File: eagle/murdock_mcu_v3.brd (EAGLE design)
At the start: 47 x 31.8 mm, 34 parts, among them IC1 MPU-9150, IC2 LT1763CS8-3.3, IC3 STM32F4XX_64, IC4 BMP085, IC5 24LC16BSN, T1 PFET, U1 USD-SOCKETNEW, X2 MURDOCK_STACK

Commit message: usb fix
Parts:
- added R7: 15k, SparkFun-Resistors:0402-RES
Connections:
- net +3V3: now also R7.1
- net +5V: now also IC3.42
- net SP_PWR: now also R7.2
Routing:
- net +5V: track 35.7 -> 56.2 mm, vias 2 -> 4
- net SP_PWR: track 20.7 -> 25.4 mm
- net +3V3: track 182.1 -> 183.5 mm
- net GND: vias 28 -> 27
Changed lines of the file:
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@@
 </element>
 <element name="C8" library="rcl" package="C0402" value="10nF" x="4.4675" y="20.49" smashed="yes" rot="R90">
-<attribute name="NAME" x="5.245" y="19.2325" size="0.8128" layer="25" font="vector" ratio="10" rot="R180"/>
+<attribute name="NAME" x="5.1675" y="21.345" size="0.8128" layer="25" font="vector" ratio="10" rot="R270"/>
 <attribute name="VALUE" x="4.7725" y="19.155" size="0.6096" layer="27" font="vector" ratio="10" rot="R90"/>
 </element>
@@
 <attribute name="NAME" x="20.095" y="17.467" size="0.8128" layer="25" font="vector" ratio="10"/>
 <attribute name="VALUE" x="22.595" y="16.963" size="1.27" layer="27"/>
+</element>
+<element name="R7" library="SparkFun-Resistors" package="0402-RES" value="15k" x="4.4" y="17.8" smashed="yes" rot="R270">
+<attribute name="NAME" x="5.0985" y="18.689" size="0.8128" layer="25" font="vector" ratio="10" rot="R270"/>
+<attribute name="VALUE" x="3.257" y="18.8795" size="0.4064" layer="27" rot="R270"/>
 </element>
 </elements>
@@
 <wire x1="39.0025" y1="12.2475" x2="37.1025" y2="12.2475" width="0.3048" layer="1"/>
 <via x="20.3" y="8.35" extent="1-16" drill="0.6"/>
-<via x="23.55" y="14.75" extent="1-16" drill="0.6"/>
 <via x="20.55" y="14.65" extent="1-16" drill="0.6"/>
 <via x="23.95" y="21.35" extent="1-16" drill="0.6"/>
@@
 <via x="32.25" y="29.8" extent="1-16" drill="0.6"/>
 <via x="36.85" y="24.5" extent="1-16" drill="0.4"/>
-<via x="24.2" y="19.2" extent="1-16" drill="0.6"/>
+<via x="24.5" y="19.1" extent="1-16" drill="0.6"/>
 <contactref element="IC4" pad="1"/>
 <via x="9.85" y="22.65" extent="1-16" drill="0.6"/>
@@
 <contactref element="X2" pad="3V3"/>
 <contactref element="C2" pad="+"/>
-<wire x1="5.715" y1="18.265" x2="5.715" y2="21.1675" width="0.6096" layer="1"/>
+<wire x1="5.715" y1="18.265" x2="5.715" y2="18.5" width="0.6096" layer="1"/>
 <contactref element="IC3" pad="48"/>
 <contactref element="IC3" pad="64"/>
@@
 <contactref element="C3" pad="1"/>
 <contactref element="U1" pad="4"/>
+<wire x1="5.715" y1="18.5" x2="5.715" y2="21.1675" width="0.6096" layer="1"/>
 <wire x1="5.715" y1="21.1675" x2="5.715" y2="23.185" width="0.6096" layer="1"/>
 <wire x1="34.4525" y1="16.0975" x2="34.4525" y2="17.1975" width="0.3048" layer="1"/>
@@
 <via x="34.8" y="8.35" extent="1-16" drill="0.4"/>
 <wire x1="4.4675" y1="21.14" x2="5.715" y2="21.1675" width="0.6096" layer="1"/>
-<wire x1="5.715" y1="21.1675" x2="5.715" y2="18.265" width="0.6096" layer="1"/>
-<wire x1="5.715" y1="18.1575" x2="5.715" y2="21.1675" width="0.6096" layer="1"/>
+<wire x1="5.715" y1="21.1675" x2="5.715" y2="18.5" width="0.6096" layer="1"/>
+<wire x1="5.715" y1="18.5" x2="5.715" y2="18.265" width="0.6096" layer="1"/>
+<wire x1="5.715" y1="18.1575" x2="5.715" y2="18.5" width="0.6096" layer="1"/>
+<wire x1="5.715" y1="18.5" x2="5.715" y2="21.1675" width="0.6096" layer="1"/>
 <wire x1="5.715" y1="18.1575" x2="7.95" y2="18.1575" width="0.6096" layer="1"/>
 <wire x1="7.95" y1="18.1575" x2="10.3" y2="18.2" width="0.6096" layer="1"/>
@@
 <wire x1="23.9" y1="23.6" x2="23.9" y2="26.665" width="0.3048" layer="1"/>
 <wire x1="23.9" y1="26.665" x2="23.935" y2="26.7" width="0.3048" layer="1"/>
+<contactref element="R7" pad="1"/>
+<wire x1="4.4" y1="18.45" x2="5.715" y2="18.45" width="0.3048" layer="1"/>
+<wire x1="5.715" y1="18.45" x2="5.715" y2="18.5" width="0.3048" layer="1"/>
 </signal>
 <signal name="+5V">
@@
 <wire x1="9.3525" y1="27.305" x2="10.3075" y2="27.305" width="0.6096" layer="16"/>
 <wire x1="10.3075" y1="27.305" x2="10.3075" y2="26.35" width="0.6096" layer="16"/>
+<contactref element="IC3" pad="42"/>
+<wire x1="26.1025" y1="9.7475" x2="24.1525" y2="9.7475" width="0.3048" layer="1"/>
+<wire x1="24.1525" y1="9.7475" x2="23.7" y2="10.2" width="0.3048" layer="1"/>
+<via x="23.7" y="10.2" extent="1-16" drill="0.4"/>
+<wire x1="23.7" y1="10.2" x2="23.7" y2="11" width="0.3048" layer="16"/>
+<wire x1="23.7" y1="11" x2="23.3" y2="11.4" width="0.3048" layer="16"/>
+<wire x1="23.3" y1="11.4" x2="23.3" y2="19.6" width="0.3048" layer="16"/>
+<wire x1="23.3" y1="19.6" x2="21.2" y2="21.7" width="0.3048" layer="16"/>
+<wire x1="21.2" y1="21.7" x2="21.2" y2="23.9" width="0.3048" layer="16"/>
+<wire x1="21.2" y1="23.9" x2="22.1" y2="24.8" width="0.3048" layer="16"/>
+<via x="22.1" y="24.8" extent="1-16" drill="0.4"/>
+<wire x1="22.1" y1="24.8" x2="20.23" y2="24.8" width="0.3048" layer="1"/>
+<wire x1="20.23" y1="24.8" x2="20.2075" y2="24.7775" width="0.3048" layer="1"/>
 </signal>
 <signal name="N$13">
@@
 <wire x1="23.75" y1="13.65" x2="24.3475" y2="14.2475" width="0.3048" layer="1"/>
 <wire x1="24.3475" y1="14.2475" x2="26.1025" y2="14.2475" width="0.3048" layer="1"/>
+<contactref element="R7" pad="2"/>
+<wire x1="4.4" y1="17.15" x2="4.6" y2="17.15" width="0.3048" layer="1"/>
+<wire x1="4.6" y1="17.15" x2="4.6" y2="13.7" width="0.3048" layer="1"/>
+<wire x1="4.6" y1="13.7" x2="5.6" y2="13.7" width="0.3048" layer="1"/>
+<wire x1="5.6" y1="13.7" x2="5.6" y2="13.65" width="0.3048" layer="1"/>
 </signal>
 <signal name="N$9">
@@
 </signal>
 </signals>
-<errors>
-</errors>
 </board>
 </drawing>

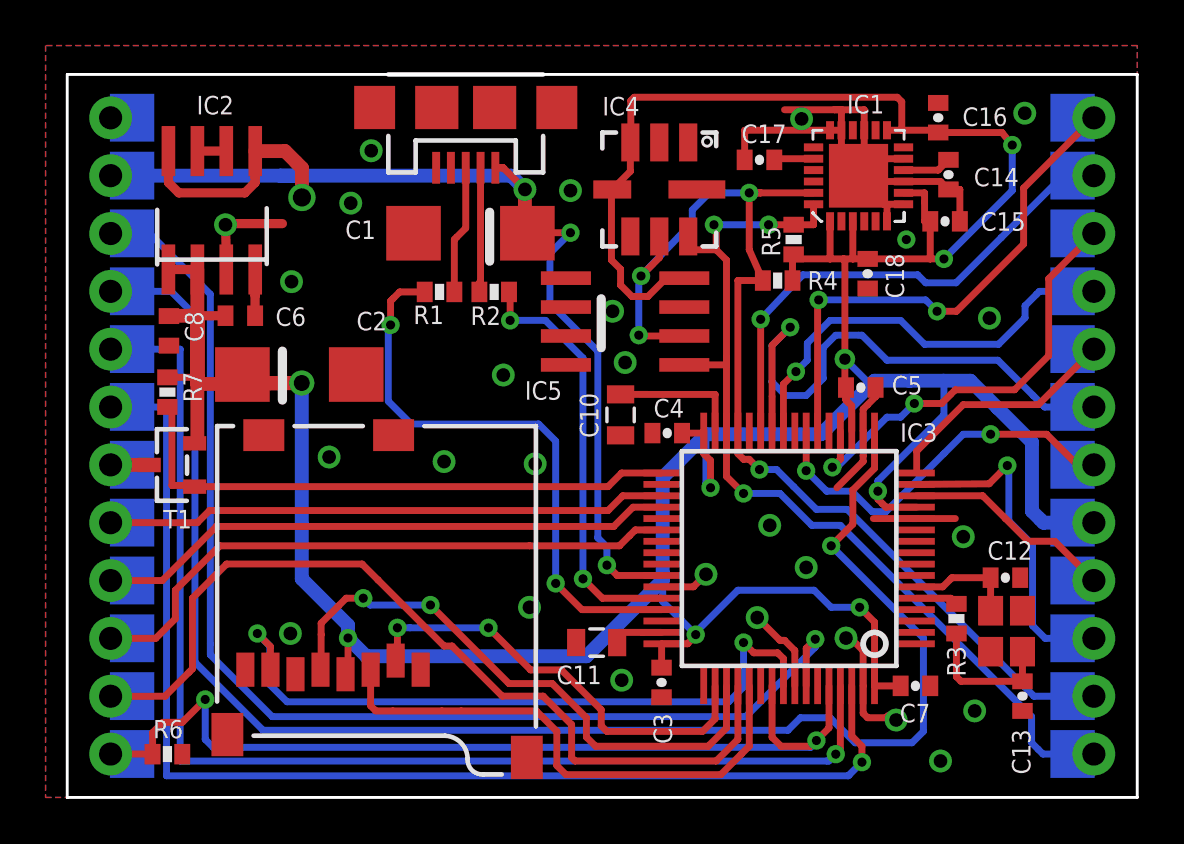
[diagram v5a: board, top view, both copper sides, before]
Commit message: moved sd card
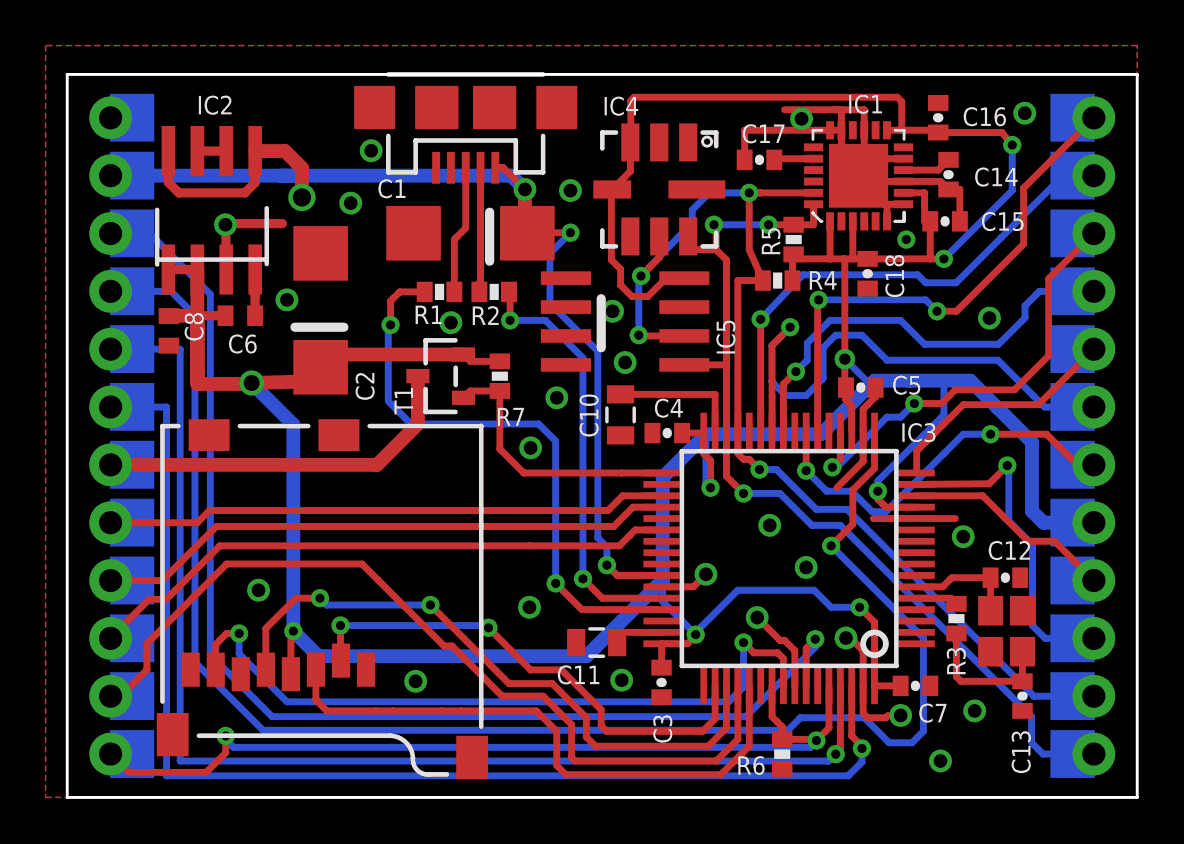
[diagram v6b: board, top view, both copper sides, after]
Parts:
- moved R6 27.0 mm to (31.4, 1.90), turned to 90 degrees
- moved R7 14.6 mm to (19.0, 18.5)
- moved T1 12.4 mm to (16.4, 18.5)
- moved C2 2.97 mm to (11.1, 21.4), turned to 90 degrees
- moved U1 2.40 mm to (4.18, 16.3)
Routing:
- net N$8: track 1.70 -> 16.3 mm
- net SP_PWR: track 25.4 -> 11.8 mm
- net +3V3: track 183.5 -> 188.8 mm
- net SD_CS: track 19.4 -> 22.0 mm
- net SCK: track 25.7 -> 28.0 mm
- net MOSI: track 23.5 -> 25.8 mm
- net SW1: track 41.7 -> 39.5 mm
- net C11: track 38.9 -> 37.8 mm
- net MISO: track 30.9 -> 31.7 mm
- net C7: track 26.9 -> 26.2 mm
